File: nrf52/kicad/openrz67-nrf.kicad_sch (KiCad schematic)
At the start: 14 parts, among them J1 Camera, J2 SWD, Q1 AO3401A, SW1 B3U-1000P, U1 E73-2G4M08S1C, U2 TLP172AM, U3 TLP172AM

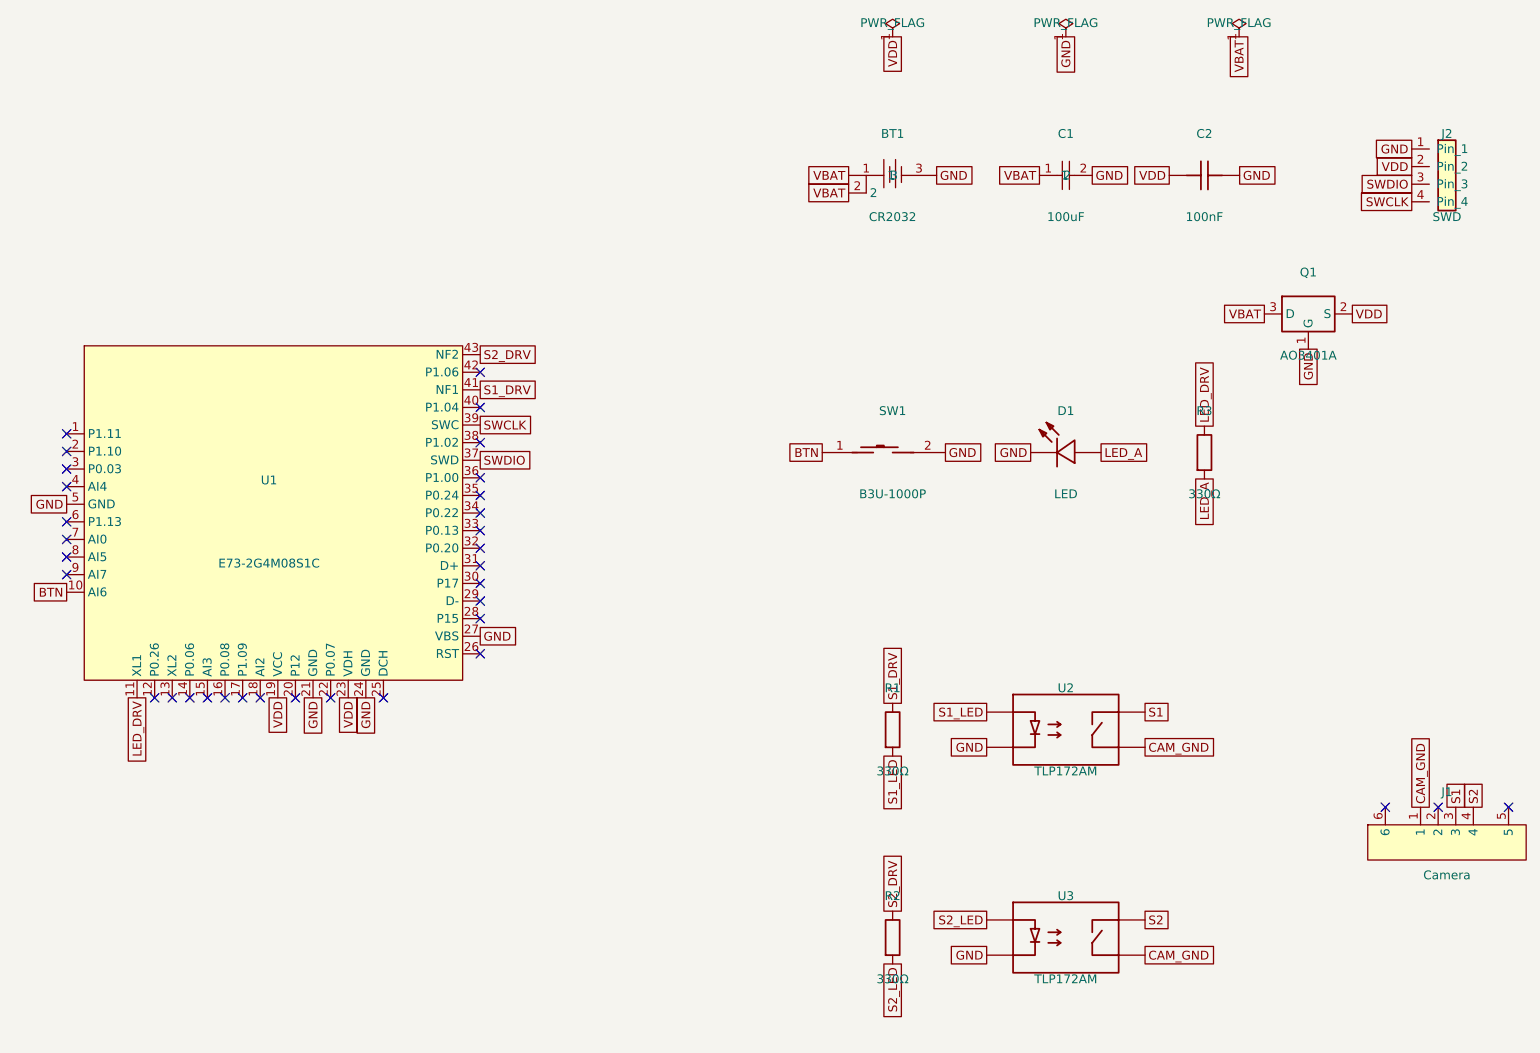
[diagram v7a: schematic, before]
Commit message: nrf52 pcb: E73-2G4M08S1F (nRF54L15) module
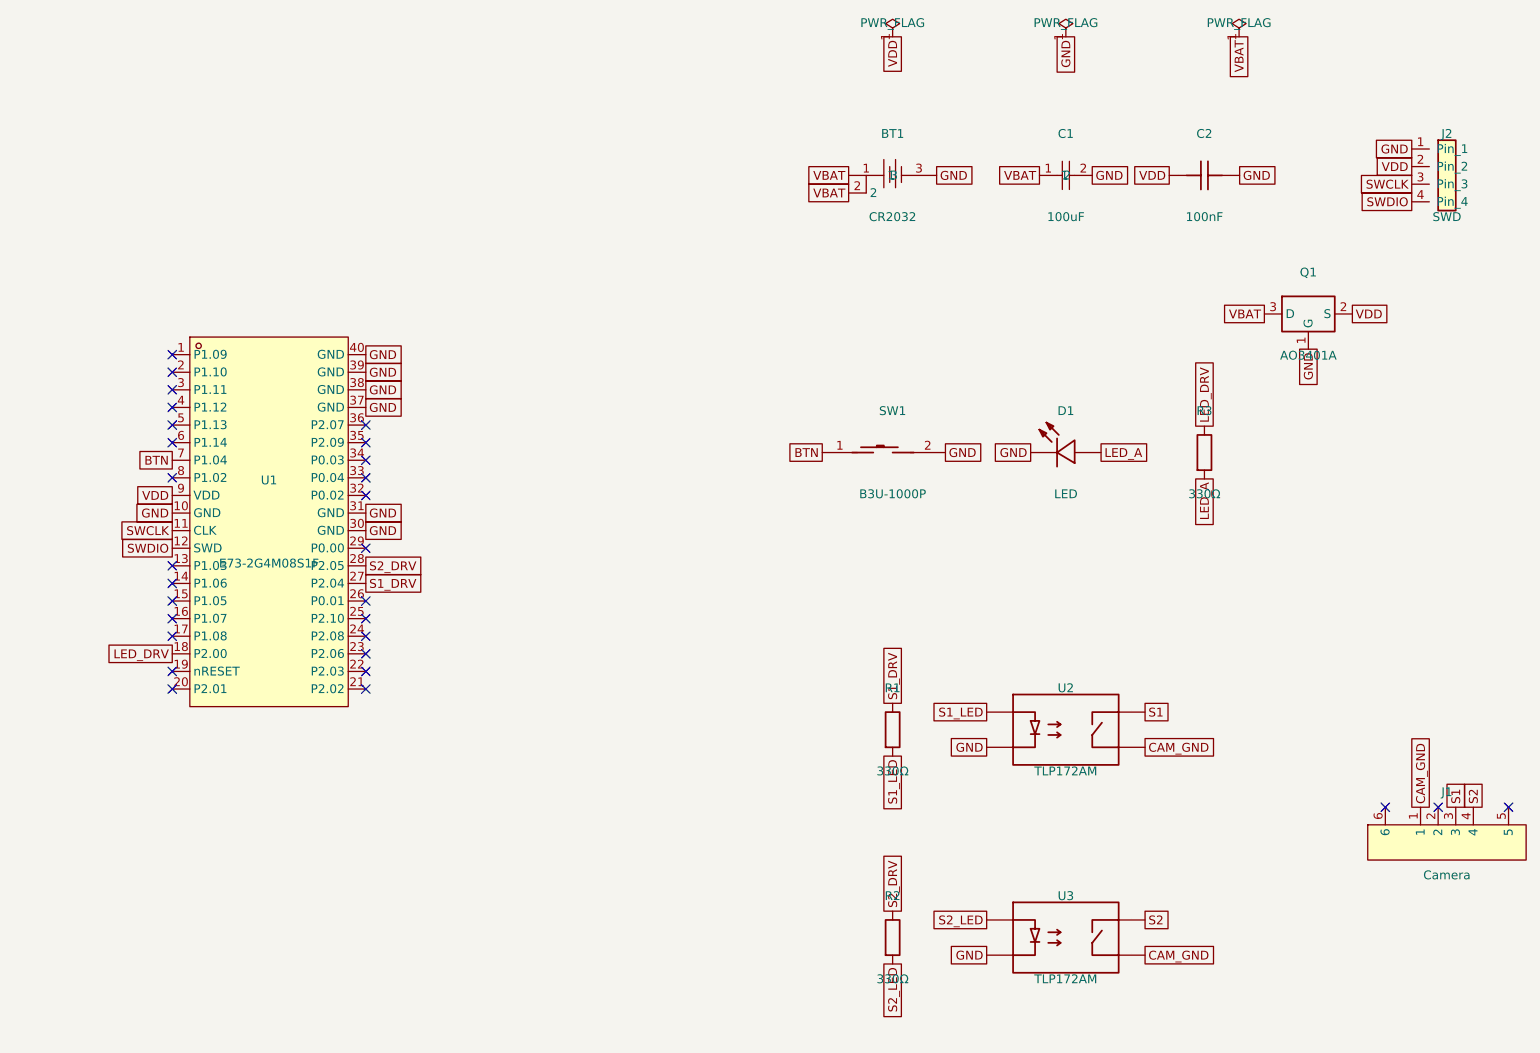
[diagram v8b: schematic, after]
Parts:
- removed U1: E73-2G4M08S1C, openrz67-nrf:WIRELM-SMD_E73-2G4M08S1C, symbol openrz67-nrf:E73-2G4M08S1C
- added U1: E73-2G4M08S1F, openrz67-nrf:WIRELM-SMD_E73-2G4M08S1F, symbol openrz67-nrf:E73-2G4M08S1F
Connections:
- net BTN: now also U1.7 (P1.04)
- net GND: now also U1.10 (GND), U1.30 (GND), U1.31 (GND), U1.37 (GND), U1.38 (GND), U1.39 (GND), U1.40 (GND)
- net LED_DRV: now also U1.18 (P2.00)
- net S1_DRV: now also U1.27 (P2.04)
- net S2_DRV: now also U1.28 (P2.05)
- net SWCLK: now also J2.3 (Pin_3), U1.11 (CLK); no longer J2.4 (Pin_4)
- net SWDIO: now also J2.4 (Pin_4), U1.12 (SWD); no longer J2.3 (Pin_3)
- net VDD: now also U1.9 (VDD)
- no-connect marks 34 -> 29
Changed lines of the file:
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@@
   (paper "A4")
   (title_block (title "OpenRZ67 trigger, nRF52 / coin cell") (rev "A") (company "openrz67"))
-  (symbol (lib_id "openrz67-nrf:E73-2G4M08S1C") (at 60 90 0) (unit 1)
+  (symbol (lib_id "openrz67-nrf:E73-2G4M08S1F") (at 60 90 0) (unit 1)
     (in_bom yes) (on_board yes) (dnp no)
     (property "Reference" "U1" (at 60 84 0)
       (effects (font (size 1.27 1.27)))
     )
-    (property "Value" "E73-2G4M08S1C" (at 60 96 0)
-      (effects (font (size 1.27 1.27)))
-    )
-    (property "Footprint" "openrz67-nrf:WIRELM-SMD_E73-2G4M08S1C" (at 60 90 0)
+    (property "Value" "E73-2G4M08S1F" (at 60 96 0)
+      (effects (font (size 1.27 1.27)))
+    )
+    (property "Footprint" "openrz67-nrf:WIRELM-SMD_E73-2G4M08S1F" (at 60 90 0)
       (effects (font (size 1.27 1.27)) hide)
     )
@@
       (effects (font (size 1.27 1.27)) hide)
     )
-    (property "Description" "nRF52840 module, ceramic antenna at the board edge" (at 60 90 0)
-      (effects (font (size 1.27 1.27)) hide)
-    )
-    (property "LCSC" "C356849" (at 60 90 0)
-      (effects (font (size 1.27 1.27)) hide)
-    )
-    (property "MPN" "E73-2G4M08S1C" (at 60 90 0)
+    (property "Description" "nRF54L15 module, PCB antenna at the board edge" (at 60 90 0)
+      (effects (font (size 1.27 1.27)) hide)
+    )
+    (property "LCSC" "C54337734" (at 60 90 0)
+      (effects (font (size 1.27 1.27)) hide)
+    )
+    (property "MPN" "E73-2G4M08S1F" (at 60 90 0)
       (effects (font (size 1.27 1.27)) hide)
     )
@@
     (pin "39")
     (pin "40")
-    (pin "41")
-    (pin "42")
-    (pin "43")
     (instances
       (project "openrz67-nrf" (path "/5d1c1d2e-0a3b-4c4d-9e5f-6a7b8c9d0e1f" (reference "U1") (unit 1)))
@@
       (effects (font (size 1.27 1.27)) hide)
     )
-    (property "Description" "SWD, SH 1.0 mm side-entry (Qwiic cable to the probe): 1 GND, 2 VDD, 3 SWDIO, 4 SWCLK" (at 230 40 0)
+    (property "Description" "SWD, SH 1.0 mm side-entry (Qwiic cable to the probe): 1 GND, 2 VDD, 3 SWCLK, 4 SWDIO" (at 230 40 0)
       (effects (font (size 1.27 1.27)) hide)
     )
@@
     (instances (project "openrz67-nrf" (path "/5d1c1d2e-0a3b-4c4d-9e5f-6a7b8c9d0e1f" (reference "#FLG3") (unit 1))))
   )
-  (global_label "GND" (shape passive) (at 30.79 87.46 180) (fields_autoplaced yes)
-    (effects (font (size 1.27 1.27)) (justify right))
-  )
-  (global_label "BTN" (shape passive) (at 30.79 100.16 180) (fields_autoplaced yes)
-    (effects (font (size 1.27 1.27)) (justify right))
-  )
-  (global_label "LED_DRV" (shape passive) (at 40.95 115.4 270) (fields_autoplaced yes)
-    (effects (font (size 1.27 1.27)) (justify right))
-  )
-  (global_label "VDD" (shape passive) (at 61.27 115.4 270) (fields_autoplaced yes)
-    (effects (font (size 1.27 1.27)) (justify right))
-  )
-  (global_label "GND" (shape passive) (at 66.35 115.4 270) (fields_autoplaced yes)
-    (effects (font (size 1.27 1.27)) (justify right))
-  )
-  (global_label "VDD" (shape passive) (at 71.43 115.4 270) (fields_autoplaced yes)
-    (effects (font (size 1.27 1.27)) (justify right))
-  )
-  (global_label "GND" (shape passive) (at 73.97 115.4 270) (fields_autoplaced yes)
-    (effects (font (size 1.27 1.27)) (justify right))
-  )
-  (global_label "GND" (shape passive) (at 90.48 106.51 0) (fields_autoplaced yes)
-    (effects (font (size 1.27 1.27)) (justify left))
-  )
-  (global_label "SWDIO" (shape passive) (at 90.48 81.11 0) (fields_autoplaced yes)
-    (effects (font (size 1.27 1.27)) (justify left))
-  )
-  (global_label "SWCLK" (shape passive) (at 90.48 76.03 0) (fields_autoplaced yes)
-    (effects (font (size 1.27 1.27)) (justify left))
-  )
-  (global_label "S1_DRV" (shape passive) (at 90.48 70.95 0) (fields_autoplaced yes)
-    (effects (font (size 1.27 1.27)) (justify left))
-  )
-  (global_label "S2_DRV" (shape passive) (at 90.48 65.87 0) (fields_autoplaced yes)
+  (global_label "BTN" (shape passive) (at 46.03 81.11 180) (fields_autoplaced yes)
+    (effects (font (size 1.27 1.27)) (justify right))
+  )
+  (global_label "VDD" (shape passive) (at 46.03 86.19 180) (fields_autoplaced yes)
+    (effects (font (size 1.27 1.27)) (justify right))
+  )
+  (global_label "GND" (shape passive) (at 46.03 88.73 180) (fields_autoplaced yes)
+    (effects (font (size 1.27 1.27)) (justify right))
+  )
+  (global_label "SWCLK" (shape passive) (at 46.03 91.27 180) (fields_autoplaced yes)
+    (effects (font (size 1.27 1.27)) (justify right))
+  )
+  (global_label "SWDIO" (shape passive) (at 46.03 93.81 180) (fields_autoplaced yes)
+    (effects (font (size 1.27 1.27)) (justify right))
+  )
+  (global_label "LED_DRV" (shape passive) (at 46.03 109.05 180) (fields_autoplaced yes)
+    (effects (font (size 1.27 1.27)) (justify right))
+  )
+  (global_label "S1_DRV" (shape passive) (at 73.97 98.89 0) (fields_autoplaced yes)
+    (effects (font (size 1.27 1.27)) (justify left))
+  )
+  (global_label "S2_DRV" (shape passive) (at 73.97 96.35 0) (fields_autoplaced yes)
+    (effects (font (size 1.27 1.27)) (justify left))
+  )
+  (global_label "GND" (shape passive) (at 73.97 91.27 0) (fields_autoplaced yes)
+    (effects (font (size 1.27 1.27)) (justify left))
+  )
+  (global_label "GND" (shape passive) (at 73.97 88.73 0) (fields_autoplaced yes)
+    (effects (font (size 1.27 1.27)) (justify left))
+  )
+  (global_label "GND" (shape passive) (at 73.97 73.49 0) (fields_autoplaced yes)
+    (effects (font (size 1.27 1.27)) (justify left))
+  )
+  (global_label "GND" (shape passive) (at 73.97 70.95 0) (fields_autoplaced yes)
+    (effects (font (size 1.27 1.27)) (justify left))
+  )
+  (global_label "GND" (shape passive) (at 73.97 68.41 0) (fields_autoplaced yes)
+    (effects (font (size 1.27 1.27)) (justify left))
+  )
+  (global_label "GND" (shape passive) (at 73.97 65.87 0) (fields_autoplaced yes)
     (effects (font (size 1.27 1.27)) (justify left))
   )
@@
     (effects (font (size 1.27 1.27)) (justify right))
   )
-  (global_label "SWDIO" (shape passive) (at 224.92 41.27 180) (fields_autoplaced yes)
-    (effects (font (size 1.27 1.27)) (justify right))
-  )
-  (global_label "SWCLK" (shape passive) (at 224.92 43.81 180) (fields_autoplaced yes)
+  (global_label "SWCLK" (shape passive) (at 224.92 41.27 180) (fields_autoplaced yes)
+    (effects (font (size 1.27 1.27)) (justify right))
+  )
+  (global_label "SWDIO" (shape passive) (at 224.92 43.81 180) (fields_autoplaced yes)
     (effects (font (size 1.27 1.27)) (justify right))
   )
@@
     (effects (font (size 1.27 1.27)) (justify right))
   )
-  (no_connect (at 30.79 77.3))
-  (no_connect (at 30.79 79.84))
-  (no_connect (at 30.79 82.38))
-  (no_connect (at 30.79 84.92))
-  (no_connect (at 30.79 90.0))
-  (no_connect (at 30.79 92.54))
-  (no_connect (at 30.79 95.08))
-  (no_connect (at 30.79 97.62))
-  (no_connect (at 43.49 115.4))
-  (no_connect (at 46.03 115.4))
-  (no_connect (at 48.57 115.4))
-  (no_connect (at 51.11 115.4))
-  (no_connect (at 53.65 115.4))
-  (no_connect (at 56.19 115.4))
-  (no_connect (at 58.73 115.4))
-  (no_connect (at 63.81 115.4))
-  (no_connect (at 68.89 115.4))
-  (no_connect (at 76.51 115.4))
-  (no_connect (at 90.48 109.05))
-  (no_connect (at 90.48 103.97))
-  (no_connect (at 90.48 101.43))
-  (no_connect (at 90.48 98.89))
-  (no_connect (at 90.48 96.35))
-  (no_connect (at 90.48 93.81))
-  (no_connect (at 90.48 91.27))
-  (no_connect (at 90.48 88.73))
-  (no_connect (at 90.48 86.19))
-  (no_connect (at 90.48 83.65))
-  (no_connect (at 90.48 78.57))
-  (no_connect (at 90.48 73.49))
-  (no_connect (at 90.48 68.41))
+  (no_connect (at 46.03 65.87))
+  (no_connect (at 46.03 68.41))
+  (no_connect (at 46.03 70.95))
+  (no_connect (at 46.03 73.49))
+  (no_connect (at 46.03 76.03))
+  (no_connect (at 46.03 78.57))
+  (no_connect (at 46.03 83.65))
+  (no_connect (at 46.03 96.35))
+  (no_connect (at 46.03 98.89))
+  (no_connect (at 46.03 101.43))
+  (no_connect (at 46.03 103.97))
+  (no_connect (at 46.03 106.51))
+  (no_connect (at 46.03 111.59))
+  (no_connect (at 46.03 114.13))
+  (no_connect (at 73.97 114.13))
+  (no_connect (at 73.97 111.59))
+  (no_connect (at 73.97 109.05))
+  (no_connect (at 73.97 106.51))
+  (no_connect (at 73.97 103.97))
+  (no_connect (at 73.97 101.43))
+  (no_connect (at 73.97 93.81))
+  (no_connect (at 73.97 86.19))
+  (no_connect (at 73.97 83.65))
+  (no_connect (at 73.97 81.11))
+  (no_connect (at 73.97 78.57))
+  (no_connect (at 73.97 76.03))
   (no_connect (at 228.73 131.19))
   (no_connect (at 238.89 131.19))
